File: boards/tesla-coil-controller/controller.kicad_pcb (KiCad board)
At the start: 2 copper layers, 157 x 138.6 mm, 331 parts, among them J1 DF40C-40DP-0.4V(51), J10 AUX 4 / 0-5V, J2 DF40C(2.0)-40DS-0.4V(51), J3 AUX 1 / 0-5V, J30 12V BATTERY / LOWER, J4 12V BATTERY / UPPER, J40 CST SECONDARY, J5 USB-C / PROGRAMMING ONLY, J50 GDT 1 PRIMARY, J51 GDT 2 PRIMARY, J60 CST 2 SECONDARY, J8 AUX 2 / 0-5V, J9 AUX 3 / 0-5V, Q50 STD80N10F7, Q51 STD80N10F7, Q52 STD80N10F7, Q53 STD80N10F7, Q54 STD80N10F7, Q55 STD80N10F7, Q56 STD80N10F7, Q57 STD80N10F7, U1 AD7606C-16BSTZ, U2 AP2112K-3.3, U3 USBLC6-2SC6, U30 LMZ14202HTZX/NOPB, U31 LMZ14202HTZX/NOPB, U40 OPA197IDBVR, U41 OPA197IDBVR, U42 TLV3501AIDBVR, U44 TPS60403DBVR, U51 UCC27282DR, U52 UCC27282DR, U53 UCC27282DR, U54 UCC27282DR, U60 OPA197IDBVR, U61 OPA197IDBVR, U62 TLV3501AIDBVR, U70 OPA197IDBVR, U71 OPA197IDBVR, U72 OPA197IDBVR, U73 OPA197IDBVR

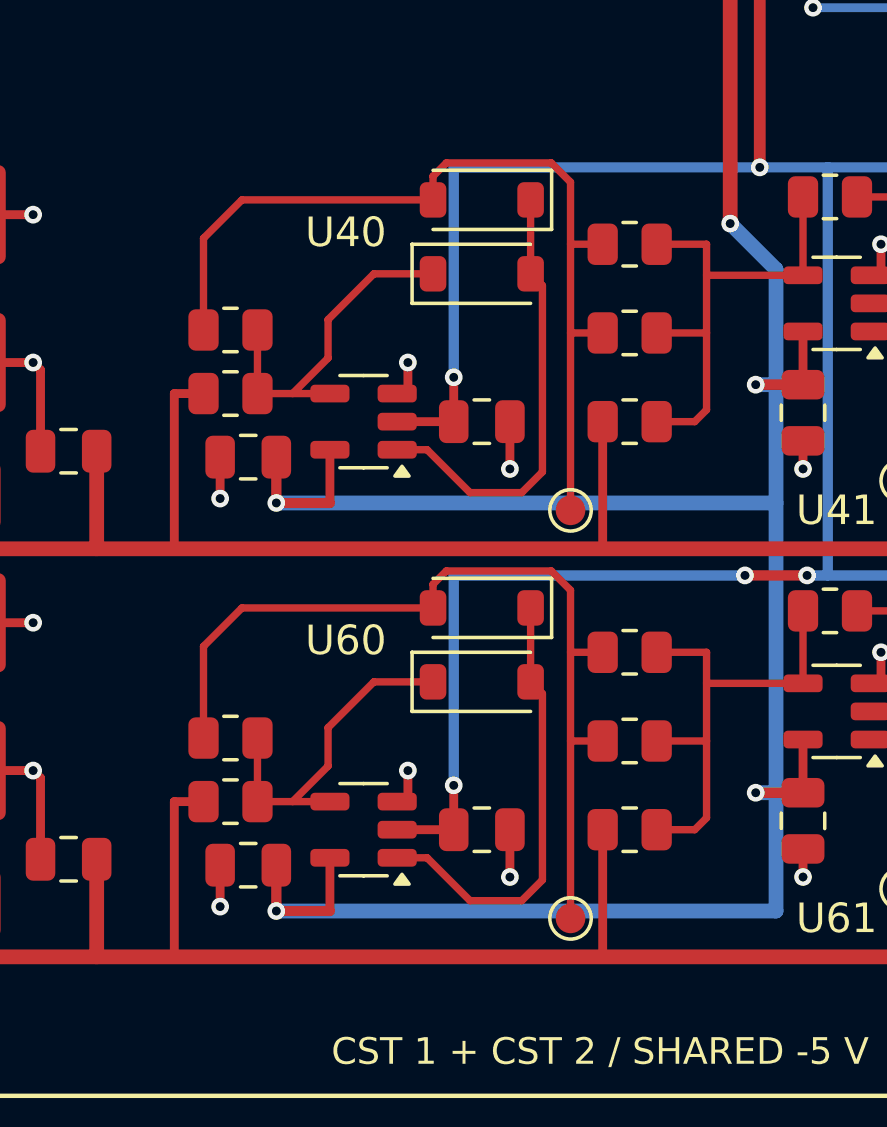
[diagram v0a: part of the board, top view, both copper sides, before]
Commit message: Put the CT HALF test points on the band-top run left of the diodes
TP41/TP61 hung at the bottom of the x=68 HALF column at y 139 / 152.8,
which forced that column to run 6 mm past the last resistor it feeds.
The HALF net already runs along the band top from R403 to the D42 pad,
so the test points now sit on that run at x=60.5, between R403 and the
diode pair, and the column stops at R406. U40/U60 reference labels moved
back under the op-amps now that the spot is free.

kicad-cli and kicadmium DRC 0/0/0; kct lint 0 open (40 flagged, 101
ignored): the two HALF loop notes re-keyed and carried over, evidence
refreshed.

Co-Authored-By: Claude Fable 5.1 <noreply@anthropic.com>
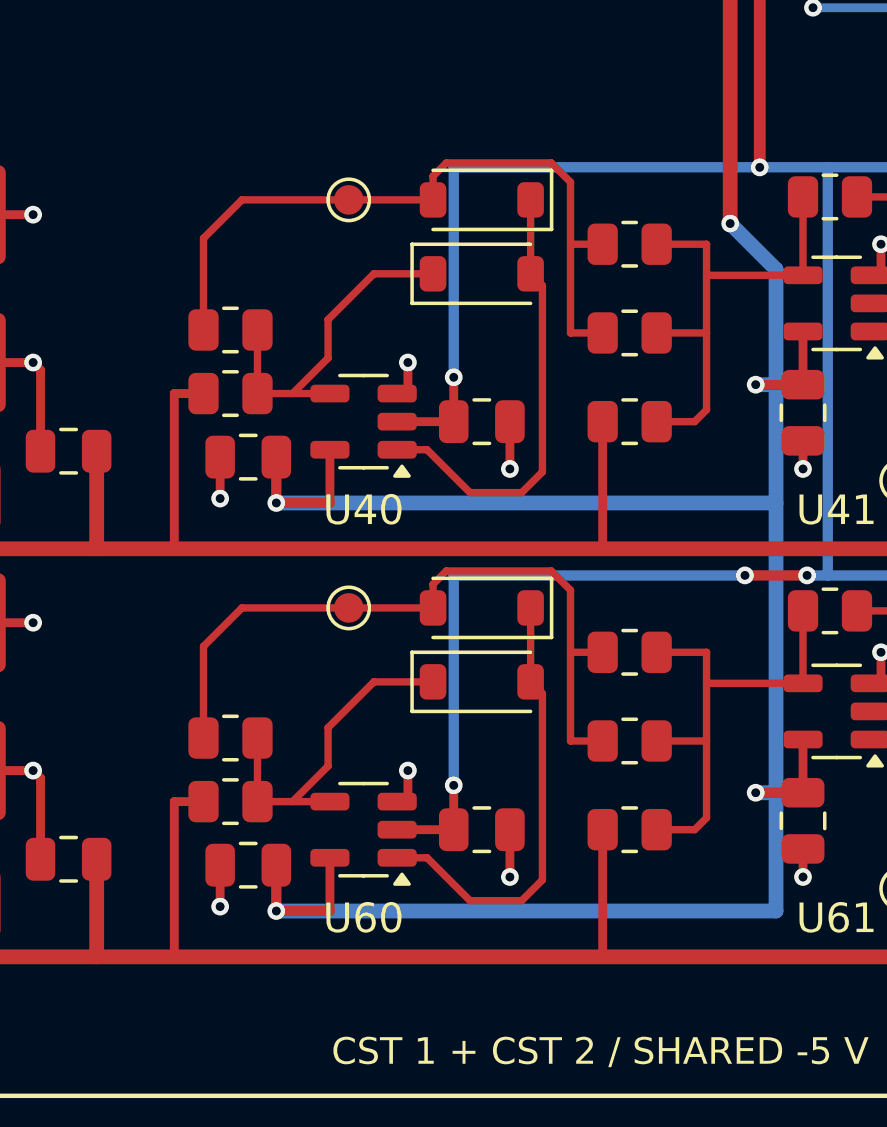
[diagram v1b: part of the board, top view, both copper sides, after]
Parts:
- moved TP41 12.9 mm to (60.5, 128.5)
- moved TP61 12.9 mm to (60.5, 142.3)
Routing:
- net CT2_HALF: track 30.6 -> 24.6 mm
- net CT1_HALF: track 30.6 -> 24.6 mm
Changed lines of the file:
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@@
 		(tags "SOT TO_SOT_SMD")
 		(property "Reference" "U60"
-			(at 0.6 6.4 0)
+			(at 0 -3 0)
 			(layer "F.SilkS")
 			(effects
@@
 	(footprint "Tesla:TestPoint_Pad_D1.0mm"
 		(layer "F.Cu")
-		(at 68 139)
+		(at 60.5 128.5)
 		(descr "SMD pad as test Point, diameter 1.0mm")
 		(tags "test point SMD pad")
 		(property "Reference" "TP41"
-			(at 0 0 0)
+			(at 0 -2.1 0)
 			(layer "F.SilkS")
 			(hide yes)
@@
 	(footprint "Tesla:TestPoint_Pad_D1.0mm"
 		(layer "F.Cu")
-		(at 68 152.8)
+		(at 60.5 142.3)
 		(descr "SMD pad as test Point, diameter 1.0mm")
 		(tags "test point SMD pad")
 		(property "Reference" "TP61"
-			(at 0 0 0)
+			(at 0 -2.1 0)
 			(layer "F.SilkS")
 			(hide yes)
@@
 		(tags "SOT TO_SOT_SMD")
 		(property "Reference" "U40"
-			(at 0.6 6.4 0)
+			(at 0 -3 0)
 			(layer "F.SilkS")
 			(effects
@@
 	(segment
 		(start 68 141.7)
-		(end 68 152.8)
+		(end 68 146.8)
 		(width 0.25)
 		(layer "F.Cu")
@@
 	(segment
 		(start 68 127.9)
-		(end 68 139)
+		(end 68 133)
 		(width 0.25)
 		(layer "F.Cu")

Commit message: Pull the bottom board edge up 4.9 mm to the mounting-hole limit
The lower-left hole H4 sits directly under the CT2 connector J60, so its
courtyard sets how far the bottom can rise: H4/H5 move from y 161.8 to
156.9 (courtyard 0.05 mm clear of J60) and the edge follows at the same
4.4 mm hole margin, 166.2 -> 161.3. GND zone outlines, the CST and GDT 2
region outlines (now at edge-0.4 like the top-left region, holes inside)
and both region labels move with it; the GDT 2 label shifts left of H5.

DRC 0/0/0 (kicad-cli and kicadmium), lint 0 open (141 exceptions
re-evidenced after the outline change, none resolved or added).
Before/after crops in docs/board-bottom-*.png.

Co-Authored-By: Claude Fable 5.1 <noreply@anthropic.com>
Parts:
- moved H4 4.90 mm to (25.0, 156.9)
- moved H5 4.90 mm to (173.0, 156.9)
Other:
- board size 157 x 138.6 mm -> 157 x 133.7 mm
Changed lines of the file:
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@@
 	(footprint "Tesla:MountingHole_3.2mm_M3"
 		(layer "F.Cu")
-		(at 25 161.8)
+		(at 25 156.9)
 		(descr "Mounting Hole 3.2mm, no annular, M3")
 		(tags "mounting hole 3.2mm no annular m3")
@@
 	(footprint "Tesla:MountingHole_3.2mm_M3"
 		(layer "F.Cu")
-		(at 173 161.8)
+		(at 173 156.9)
 		(descr "Mounting Hole 3.2mm, no annular, M3")
 		(tags "mounting hole 3.2mm no annular m3")
@@
 	)
 	(gr_line
-		(start 20.8 158.8)
+		(start 20.8 160.9)
 		(end 20.8 120)
 		(stroke
@@
 	(gr_line
 		(start 114 120)
-		(end 114 158.8)
+		(end 114 160.9)
 		(stroke
 			(width 0.15)
@@
 	)
 	(gr_line
-		(start 114 158.8)
-		(end 20.8 158.8)
+		(start 114 160.9)
+		(end 20.8 160.9)
 		(stroke
 			(width 0.15)
@@
 	)
 	(gr_line
-		(start 116.5 158)
+		(start 116.5 160.9)
 		(end 116.5 103)
 		(stroke
@@
 	(gr_line
 		(start 177 103)
-		(end 177 158)
+		(end 177 160.9)
 		(stroke
 			(width 0.15)
@@
 	)
 	(gr_line
-		(start 177 158)
-		(end 116.5 158)
+		(start 177 160.9)
+		(end 116.5 160.9)
 		(stroke
 			(width 0.15)
@@
 	)
 	(gr_line
-		(start 20.4 166.2)
+		(start 20.4 161.3)
 		(end 20.4 27.6)
 		(stroke
@@
 	(gr_line
 		(start 177.4 27.6)
-		(end 177.4 166.2)
+		(end 177.4 161.3)
 		(stroke
 			(width 0.05)
@@
 	)
 	(gr_line
-		(start 177.4 166.2)
-		(end 20.4 166.2)
+		(start 177.4 161.3)
+		(end 20.4 161.3)
 		(stroke
 			(width 0.05)
@@
 	)
 	(gr_text "CST 1 + CST 2 / SHARED -5 V"
-		(at 69 157.3 0)
+		(at 69 159.4 0)
 		(layer "F.SilkS")
 		(effects
@@
 		)
 	)
-	(gr_text "GDT 1"
-		(at 169 100.5 0)
+	(gr_text "GDT 2"
+		(at 166 159.4 0)
 		(layer "F.SilkS")
 		(effects
@@
 		)
 	)
-	(gr_text "GDT 2"
-		(at 169 155.5 0)
+	(gr_text "GDT 1"
+		(at 169 100.5 0)
 		(layer "F.SilkS")
 		(effects
@@
 		(polygon
 			(pts
-				(xy 20.75 27.95) (xy 177.05 27.95) (xy 177.05 165.85) (xy 20.75 165.85)
+				(xy 20.75 27.95) (xy 177.05 27.95) (xy 177.05 160.95) (xy 20.75 160.95)
 			)
 		)
@@
 		(polygon
 			(pts
-				(xy 20.75 27.95) (xy 177.05 27.95) (xy 177.05 165.85) (xy 20.75 165.85)
+				(xy 20.75 27.95) (xy 177.05 27.95) (xy 177.05 160.95) (xy 20.75 160.95)
 			)
 		)

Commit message: Drop the -5V_CT feed straight from C423 to the CT1 bus
The -5V feed left C423 at (60.25,116), ran 12 mm east along y 118.75,
dropped at x 74.4 to a via in the middle of the CT1 -5V bus, and the bus
then ran back west to x 64.05. The strip between the charge pump and the
CT1 band is empty there, so the feed now goes down from the C423 pad to
(60.25,122.4), 45 degrees to a via at (64.05,126.2), and joins the bus's
west vertical, which is extended up to the via as one segment. Five
tracks and a via removed, three tracks and a via added; about 8 mm of
copper and the mid-bus doubling back are gone.

DRC 0/0/0 (kicad-cli and kicadmium), lint 0 open. The two width-step
waivers at the C423 pad re-keyed and were carried over with their
original reason; evidence refreshed on the rest.
Before/after crops in docs/neg5v-feed-*.png.

Co-Authored-By: Claude Fable 5.1 <noreply@anthropic.com>
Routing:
- net -5V_CT: track 185.2 -> 174.0 mm
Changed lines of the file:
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@@
-	)
-	(segment
-		(start 74.4 119.75)
-		(end 74.4 127.4)
-		(width 0.4)
-		(layer "F.Cu")
-		(net "-5V_CT")
 	)
 	(segment
@@
 	)
 	(segment
-		(start 60.25 116)
-		(end 60.25 117.4)
-		(width 0.4)
-		(layer "F.Cu")
-		(net "-5V_CT")
-	)
-	(segment
 		(start 44.11 105.7)
 		(end 46 105.7)
@@
 	)
 	(segment
-		(start 61.6 118.75)
-		(end 73.4 118.75)
+		(start 60.25 116)
+		(end 60.25 122.4)
+		(width 0.4)
+		(layer "F.Cu")
+		(net "-5V_CT")
+	)
+	(segment
+		(start 60.25 122.4)
+		(end 64.05 126.2)
 		(width 0.4)
 		(layer "F.Cu")
@@
 	)
 	(segment
-		(start 73.4 118.75)
-		(end 74.4 119.75)
-		(width 0.4)
-		(layer "F.Cu")
-		(net "-5V_CT")
-	)
-	(segment
 		(start 44.11 78.7)
 		(end 45.4 78.7)
@@
 	)
 	(segment
-		(start 60.25 117.4)
-		(end 61.6 118.75)
-		(width 0.4)
-		(layer "F.Cu")
-		(net "-5V_CT")
-	)
-	(segment
 		(start 45.8625 108.05)
 		(end 44.11 108.05)
@@
 	)
 	(via
-		(at 74.4 127.4)
-		(size 0.6)
-		(drill 0.3)
-		(layers "F.Cu" "B.Cu")
-		(net "-5V_CT")
-	)
-	(via
 		(at 64.05 134.5)
 		(size 0.6)
@@
 	(via
 		(at 76 141.2)
+		(size 0.6)
+		(drill 0.3)
+		(layers "F.Cu" "B.Cu")
+		(net "-5V_CT")
+	)
+	(via
+		(at 64.05 126.2)
 		(size 0.6)
 		(drill 0.3)
@@
 	)
 	(segment
-		(start 64.05 127.4)
+		(start 64.05 126.2)
 		(end 64.05 134.5)
 		(width 0.35)

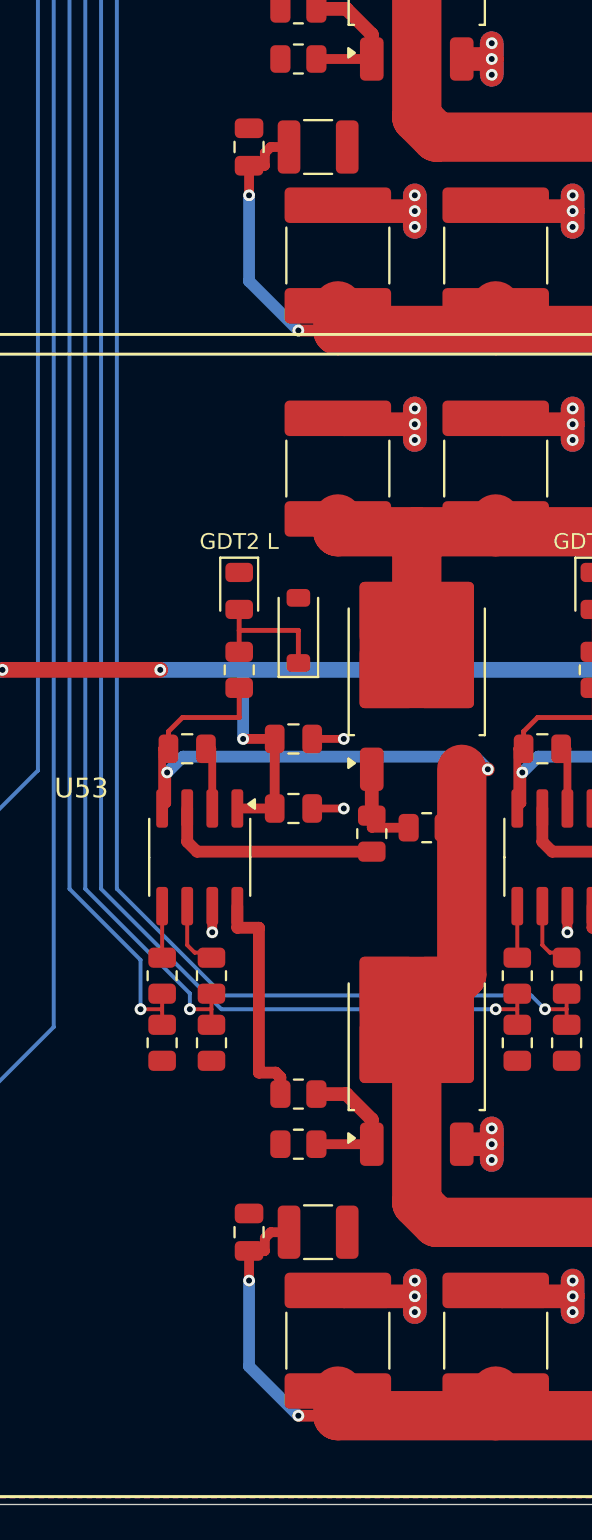
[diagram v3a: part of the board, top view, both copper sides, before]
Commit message: Remove the redundant 2.2uF/100nF bypass pairs beside both GDT bridges
C527/C528 (GDT 1) and C567/C568 (GDT 2) sat beside the eight-part
22uF 2220 reservoir banks and were fed from the VBAT bus by a back-side
detour (via, B.Cu run, via) per bridge. Eight 2220 MLCCs in parallel are
already within a few millimetres of each bridge and have lower combined
inductance than a single 0805 or 1210, so the small parts were neither
closer nor lower impedance at any frequency. Removed rather than
rerouted.

Circuit contract (docs/circuit.json) drops the four parts; the routing
recipe drops their placements, pads and the 20 detour copper objects,
lists them as removed footprints and carries the new contract hash. The
output-stage schematic block no longer draws the "Local bypass" bank;
schematic, symbol library and PDF regenerated. OUTPUT-STAGE.md and
CERAMIC-RESERVOIRS.md updated (the latter previously said to keep these
parts).

ERC 0, DRC 0/0 with 0 parity issues (kicad-cli and kicadmium), lint
0 open; the eight width-step waivers at the removed feeds resolved and
were pruned (141 -> 133 exceptions). Before/after crops in
docs/gdt-bypass-caps-*.png.

Co-Authored-By: Claude Fable 5.1 <noreply@anthropic.com>
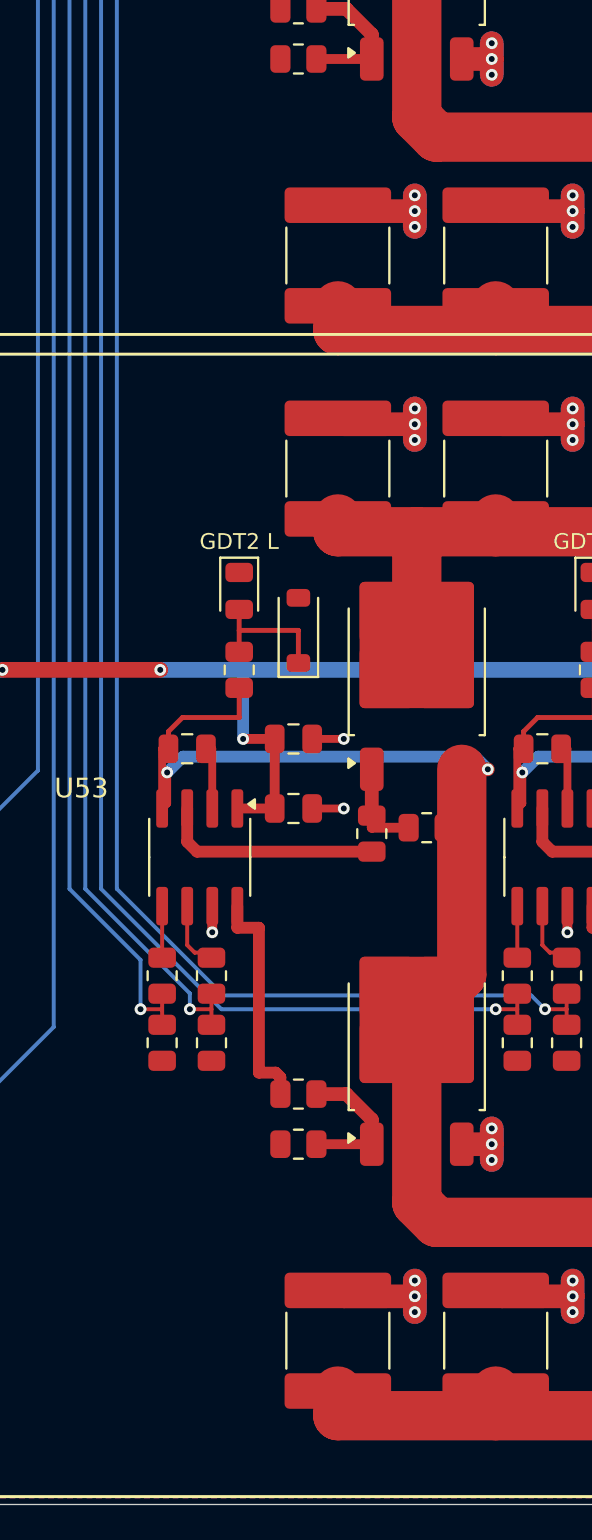
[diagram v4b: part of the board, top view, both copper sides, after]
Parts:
- removed C527, C567: 2.2uF 50V X7R, Tesla:C_1210_3225Metric
- removed C528, C568: 100nF 50V, Tesla:C_0805_2012Metric
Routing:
- net VBAT_24V: track 591.3 -> 563.0 mm, vias 16 -> 12
